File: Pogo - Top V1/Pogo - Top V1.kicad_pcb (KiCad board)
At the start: 2 copper layers, 101.5 x 101.5 mm, 1 part, among them J1 Conn_01x02_Socket

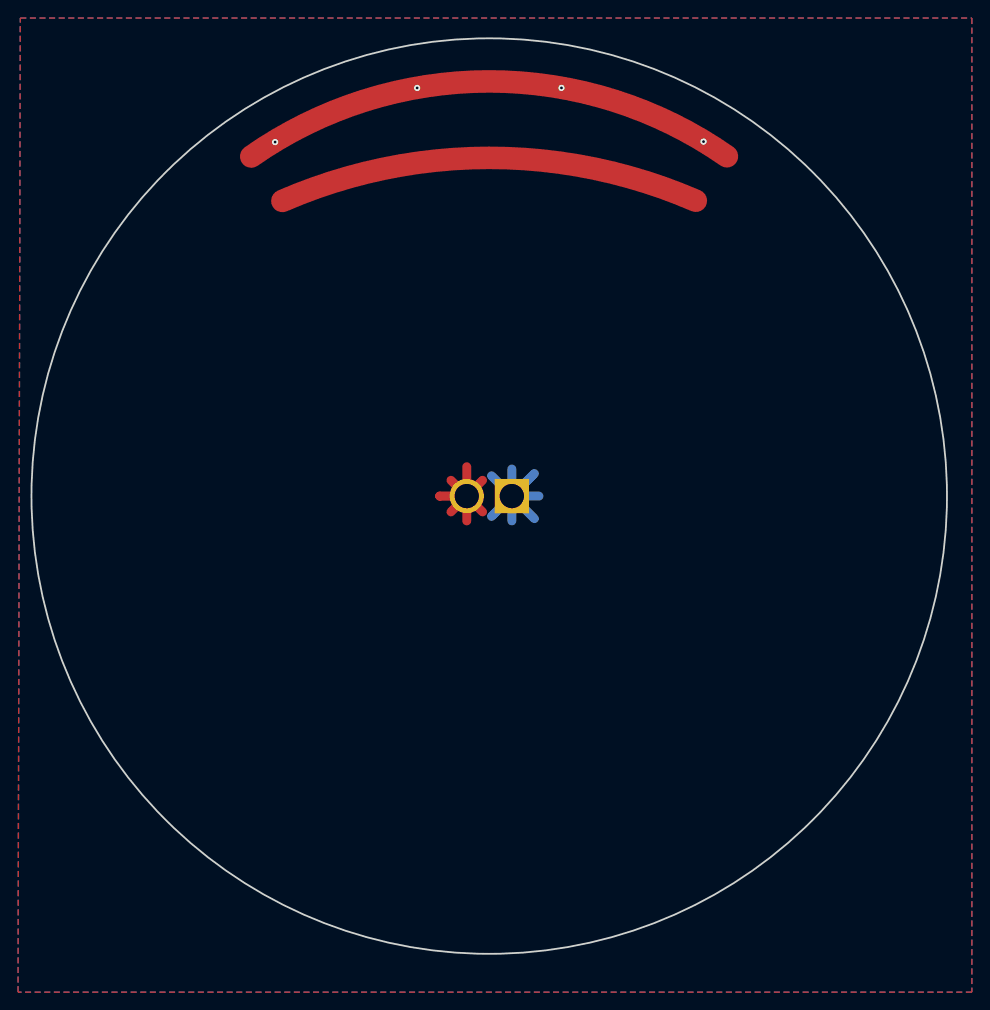
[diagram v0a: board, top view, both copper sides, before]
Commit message: Made top board the pogo board and bulkhead the pad board.
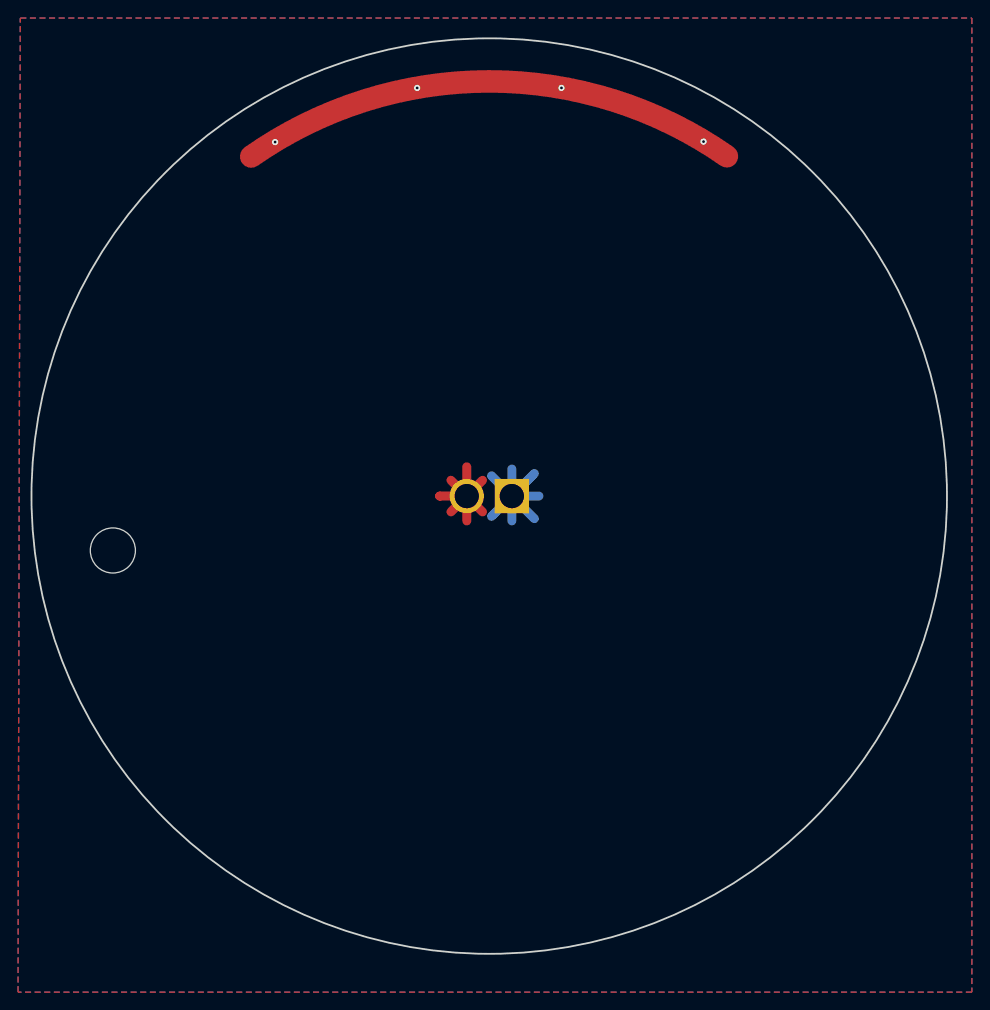
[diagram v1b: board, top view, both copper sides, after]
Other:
- outline, holes or cut-outs redrawn
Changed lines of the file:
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@@
 	(gr_arc
 		(start 123.601744 62.352334)
-		(mid 149.967868 54.025006)
+		(mid 149.967868 54.025005)
 		(end 176.342091 62.326648)
 		(stroke
@@
 	)
 	(gr_arc
+		(start 123.601744 62.352335)
+		(mid 149.967868 54.025006)
+		(end 176.342091 62.326649)
+		(stroke
+			(width 2.5)
+			(type default)
+		)
+		(layer "F.Mask")
+	)
+	(gr_arc
 		(start 127.053616 67.277011)
-		(mid 149.971995 62.500007)
+		(mid 149.971995 62.500006)
 		(end 172.895017 67.254685)
 		(stroke
@@
 			(type default)
 		)
-		(layer "F.Cu")
-		(net 2)
+		(layer "F.Mask")
+	)
+	(gr_line
+		(start 149.969932 58.262507)
+		(end 155.969919 58.250045)
+		(stroke
+			(width 0.1)
+			(type default)
+		)
+		(layer "Dwgs.User")
+	)
+	(gr_line
+		(start 108.262511 100.030595)
+		(end 108.262511 106.030595)
+		(stroke
+			(width 0.1)
+			(type default)
+		)
+		(layer "Dwgs.User")
 	)
 	(gr_circle
-		(center 150 62.5)
-		(end 151.05 62.5)
+		(center 109.6 108.6)
+		(end 109.6 108.6)
 		(stroke
 			(width 0.1)
-			(type solid)
+			(type default)
 		)
-		(fill solid)
-		(layer "F.Mask")
+		(fill none)
+		(layer "Dwgs.User")
 	)
-	(gr_circle
-		(center 150 54)
-		(end 151.05 54)
+	(gr_line
+		(start 149.969932 58.262507)
+		(end 143.969945 58.249836)
+		(stroke
+			(width 0.1)
+			(type default)
+		)
+		(layer "Dwgs.User")
+	)
+	(gr_line
+		(start 150 100)
+		(end 108.262511 100.030595)
+		(stroke
+			(width 0.1)
+			(type default)
+		)
+		(layer "Dwgs.User")
+	)
+	(gr_line
+		(start 149.971995 62.500007)
+		(end 149.967868 54.025006)
 		(stroke
 			(width 0.2)
-			(type solid)
+			(type default)
 		)
-		(fill solid)
-		(layer "F.Mask")
-	)
-	(gr_circle
-		(center 172.895017 67.254685)
-		(end 173.955677 67.254685)
-		(stroke
-			(width 0.1)
-			(type solid)
-		)
-		(fill solid)
-		(layer "F.Mask")
-	)
-	(gr_circle
-		(center 123.601744 62.352334)
-		(end 124.651744 62.352334)
-		(stroke
-			(width 0.2)
-			(type solid)
-		)
-		(fill solid)
-		(layer "F.Mask")
-	)
-	(gr_circle
-		(center 176.342091 62.326648)
-		(end 177.392091 62.326648)
-		(stroke
-			(width 0.2)
-			(type solid)
-		)
-		(fill solid)
-		(layer "F.Mask")
-	)
-	(gr_circle
-		(center 127.053616 67.277011)
-		(end 128.103616 67.277011)
-		(stroke
-			(width 0.1)
-			(type solid)
-		)
-		(fill solid)
-		(layer "F.Mask")
+		(layer "Dwgs.User")
 	)
 	(gr_circle
@@
 		(layer "Edge.Cuts")
 	)
+	(gr_circle
+		(center 108.262511 106.030595)
+		(end 110.762511 106.030595)
+		(stroke
+			(width 0.1)
+			(type default)
+		)
+		(fill none)
+		(layer "Edge.Cuts")
+	)
+	(dimension
+		(type aligned)
+		(layer "Dwgs.User")
+		(pts
+			(xy 149.969932 58.262507) (xy 150 100)
+		)
+		(height 0.00974)
+		(gr_text "41.7375 mm"
+			(at 151.125226 79.130433 270.0412763)
+			(layer "Dwgs.User")
+			(effects
+				(font
+					(size 1 1)
+					(thickness 0.15)
+				)
+			)
+		)
+		(format
+			(prefix "")
+			(suffix "")
+			(units 3)
+			(units_format 1)
+			(precision 4)
+		)
+		(style
+			(thickness 0.1)
+			(arrow_length 1.27)
+			(text_position_mode 0)
+			(extension_height 0.58642)
+			(extension_offset 0.5) keep_text_aligned)
+	)
 	(via

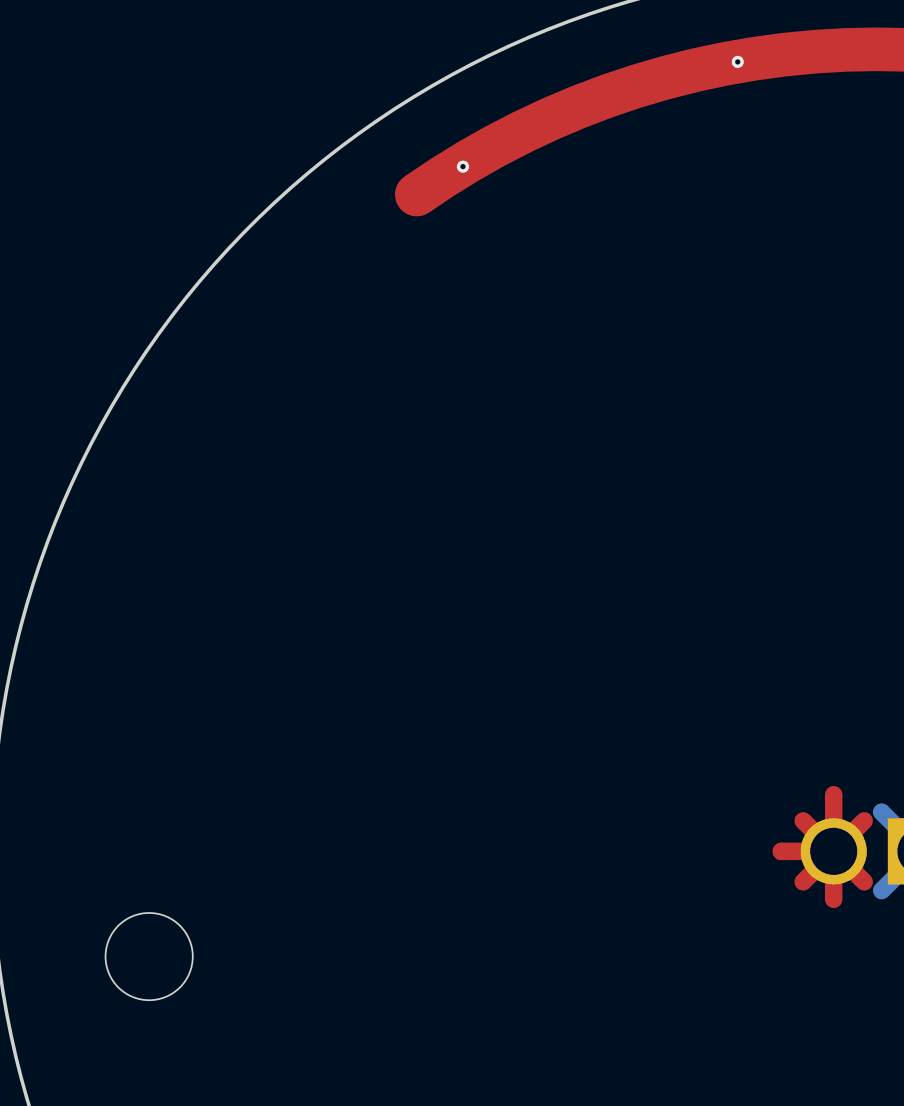
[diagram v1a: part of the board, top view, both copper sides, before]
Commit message: Fixed alingment pin placement and sizing for pogo and pad boards.
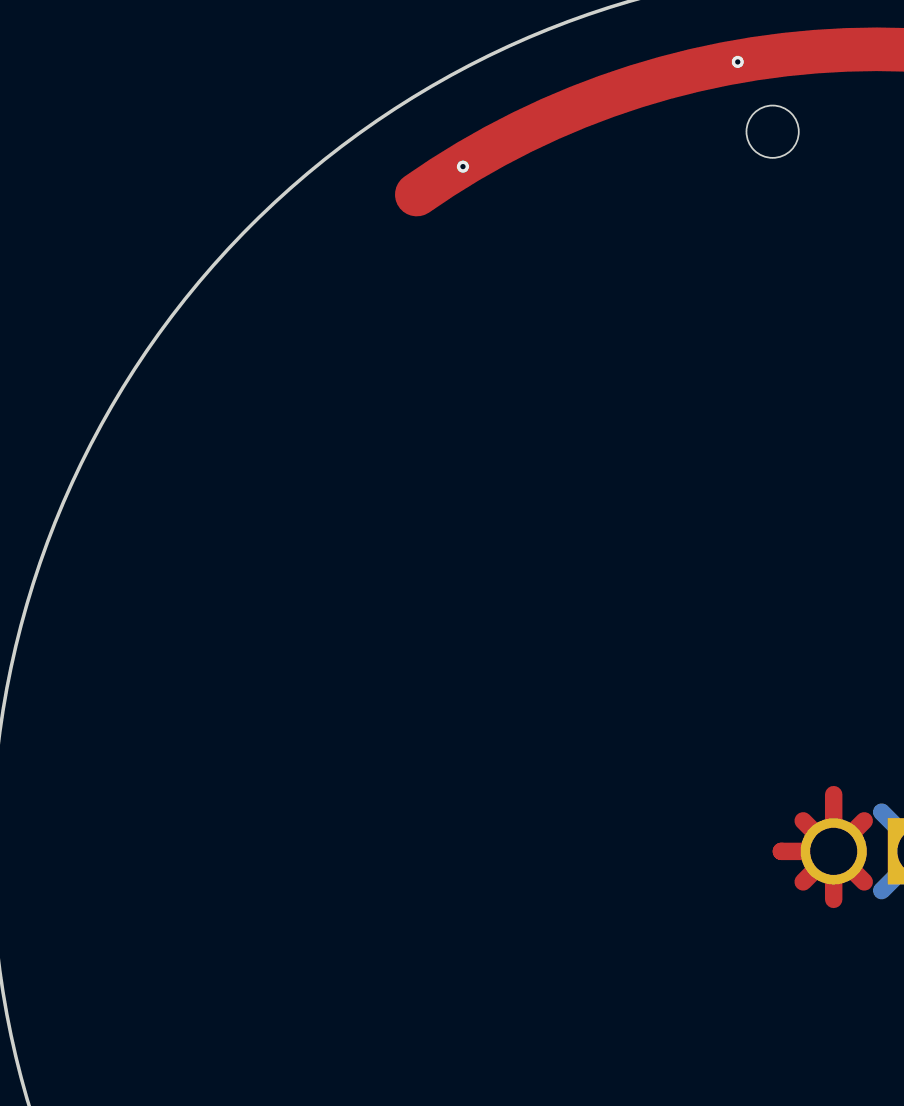
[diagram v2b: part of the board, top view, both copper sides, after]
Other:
- outline, holes or cut-outs redrawn
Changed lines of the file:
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@@
 		(layer "F.Mask")
-	)
-	(gr_line
-		(start 149.969932 58.262507)
-		(end 155.969919 58.250045)
-		(stroke
-			(width 0.1)
-			(type default)
-		)
-		(layer "Dwgs.User")
-	)
-	(gr_line
-		(start 108.262511 100.030595)
-		(end 108.262511 106.030595)
-		(stroke
-			(width 0.1)
-			(type default)
-		)
-		(layer "Dwgs.User")
 	)
 	(gr_circle
@@
 	)
 	(gr_line
-		(start 149.969932 58.262507)
-		(end 143.969945 58.249836)
+		(start 150 100)
+		(end 144 58.5)
 		(stroke
 			(width 0.1)
-			(type default)
-		)
-		(layer "Dwgs.User")
-	)
-	(gr_line
-		(start 150 100)
-		(end 108.262511 100.030595)
-		(stroke
-			(width 0.1)
-			(type default)
-		)
-		(layer "Dwgs.User")
-	)
-	(gr_line
-		(start 149.971995 62.500007)
-		(end 149.967868 54.025006)
-		(stroke
-			(width 0.2)
 			(type default)
 		)
@@
 	)
 	(gr_circle
-		(center 108.262511 106.030595)
-		(end 110.762511 106.030595)
+		(center 144 58.75)
+		(end 145.5 58.75)
 		(stroke
 			(width 0.1)
@@
 		(layer "Edge.Cuts")
 	)
-	(dimension
-		(type aligned)
-		(layer "Dwgs.User")
-		(pts
-			(xy 149.969932 58.262507) (xy 150 100)
-		)
-		(height 0.00974)
-		(gr_text "41.7375 mm"
-			(at 151.125226 79.130433 270.0412763)
-			(layer "Dwgs.User")
-			(effects
-				(font
-					(size 1 1)
-					(thickness 0.15)
-				)
-			)
-		)
-		(format
-			(prefix "")
-			(suffix "")
-			(units 3)
-			(units_format 1)
-			(precision 4)
-		)
-		(style
-			(thickness 0.1)
-			(arrow_length 1.27)
-			(text_position_mode 0)
-			(extension_height 0.58642)
-			(extension_offset 0.5) keep_text_aligned)
-	)
 	(via
